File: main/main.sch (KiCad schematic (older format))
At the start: 9 parts, among them J1 DIN41524-MIDI-IN, J2 AudioJack3, J3 Conn_02x10_Odd_Even, U1 6N138, U2 EFM32GG990F1024, U3 EFM32GG990F1024

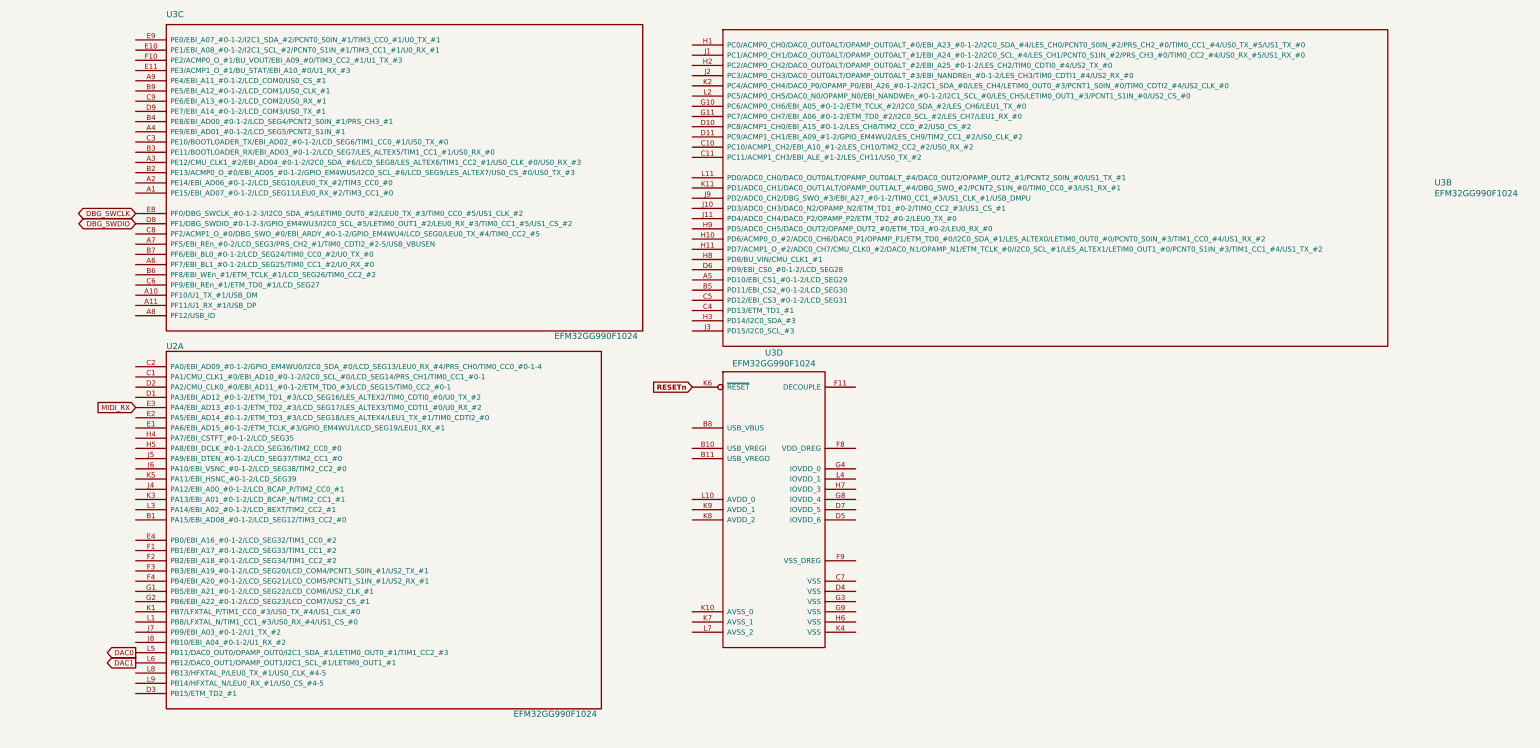
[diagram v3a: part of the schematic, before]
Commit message: Add EFM32GG component library
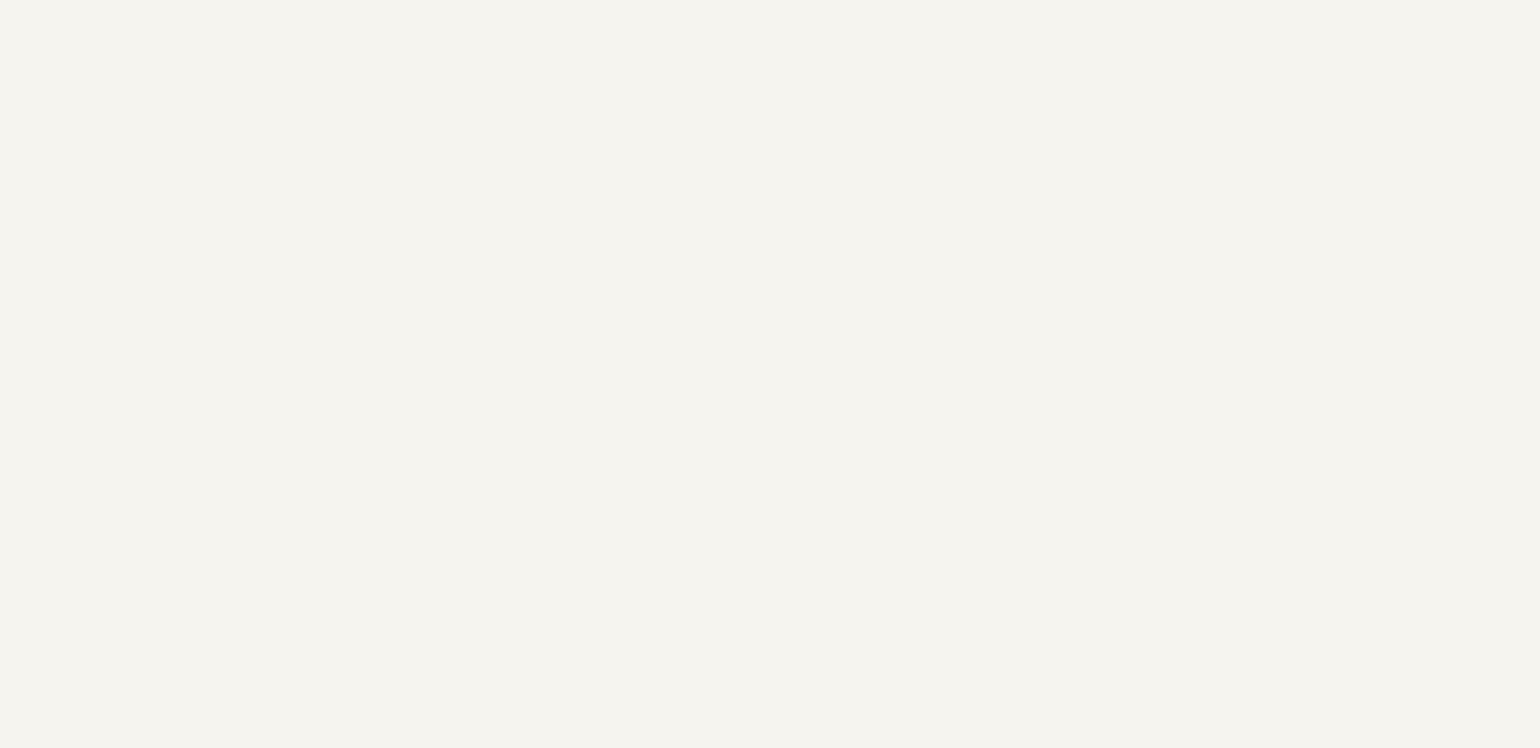
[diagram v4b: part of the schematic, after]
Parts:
- removed U2, U3: EFM32GG990F1024, symbol energymicro-efm32:EFM32GG990F1024
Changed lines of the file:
@@
 Wire Wire Line
 	2700 4800 2800 4800
-$Comp
-L energymicro-efm32:EFM32GG990F1024 U2
-U 1 1 6137537F
-P 11850 4000
-F 0 "U2" H 12150 4200 60  0000 L CNN
-F 1 "EFM32GG990F1024" H 15550 600 60  0000 L CNN
-F 2 "" H 11850 4000 50  0001 C CNN
-F 3 "http://www.energymicro.com/downloads/datasheets" H 11850 4000 50  0001 C CNN
-	1    11850 4000
-	1    0    0    -1
-$EndComp
-Text GLabel 11850 6800 0    50   Output ~ 0
-DAC0
-Text GLabel 11850 6900 0    50   Output ~ 0
-DAC1
 Text GLabel 2800 4600 0    50   Input ~ 0
 DAC0
@@
 Wire Notes Line
 	4250 3400 4250 550
-Text GLabel 11850 4400 0    50   Input ~ 0
-MIDI_RX
-$Comp
-L energymicro-efm32:EFM32GG990F1024 U3
-U 3 1 61390272
-P 11850 800
-F 0 "U3" H 12150 1050 60  0000 L CNN
-F 1 "EFM32GG990F1024" H 15950 -2100 60  0000 L CNN
-F 2 "" H 11850 800 50  0001 C CNN
-F 3 "http://www.energymicro.com/downloads/datasheets" H 11850 800 50  0001 C CNN
-	3    11850 800
-	1    0    0    -1
-$EndComp
-Text GLabel 11850 2500 0    50   BiDi ~ 0
-DBG_SWCLK
-Text GLabel 11850 2600 0    50   BiDi ~ 0
-DBG_SWDIO
 Wire Notes Line
 	550  7650 4250 7650
@@
 NoConn ~ 2750 6600
 NoConn ~ 2750 6900
-$Comp
-L energymicro-efm32:EFM32GG990F1024 U3
-U 2 1 613B0438
-P 17300 850
-F 0 "U3" H 24568 -497 60  0000 L CNN
-F 1 "EFM32GG990F1024" H 24568 -603 60  0000 L CNN
-F 2 "" H 17300 850 50  0001 C CNN
-F 3 "http://www.energymicro.com/downloads/datasheets" H 17300 850 50  0001 C CNN
-	2    17300 850
-	1    0    0    -1
-$EndComp
-$Comp
-L energymicro-efm32:EFM32GG990F1024 U3
-U 4 1 613B35C7
-P 17300 4200
-F 0 "U3" H 18100 4537 60  0000 C CNN
-F 1 "EFM32GG990F1024" H 18100 4431 60  0000 C CNN
-F 2 "" H 17300 4200 50  0001 C CNN
-F 3 "http://www.energymicro.com/downloads/datasheets" H 17300 4200 50  0001 C CNN
-	4    17300 4200
-	1    0    0    -1
-$EndComp
-Text GLabel 17300 4200 0    50   Input ~ 10
-RESETn
 Text GLabel 2750 7100 0    50   Output ~ 10
 RESETn

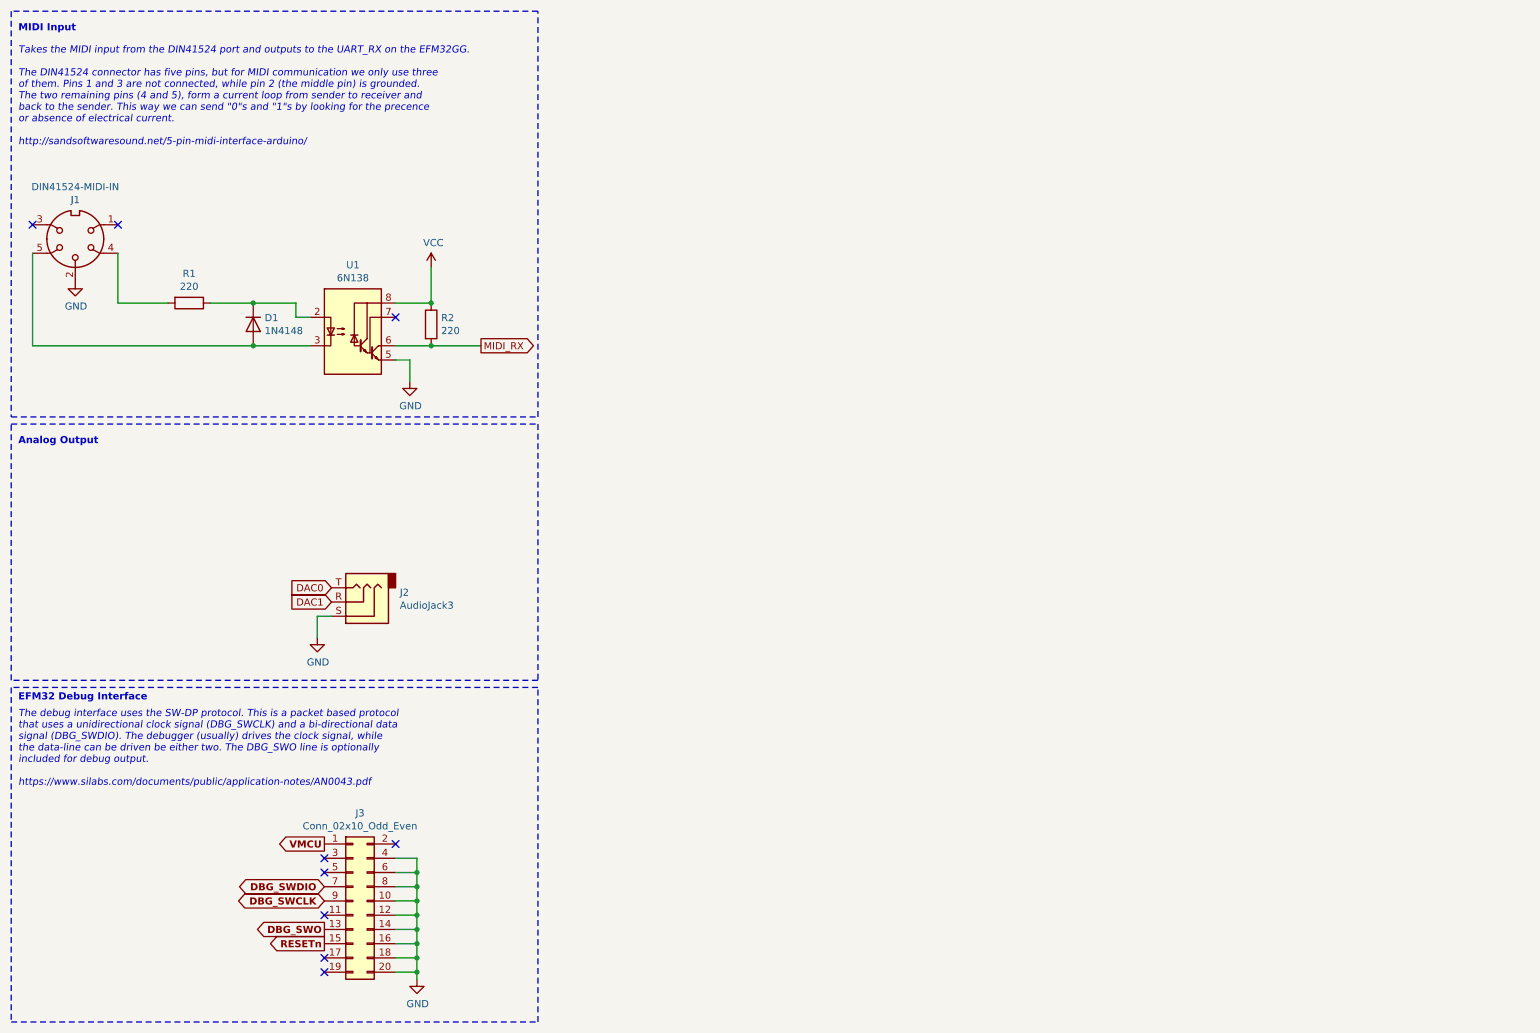
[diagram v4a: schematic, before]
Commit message: Place separate parts in hierarchical sheets, connect in main schematic
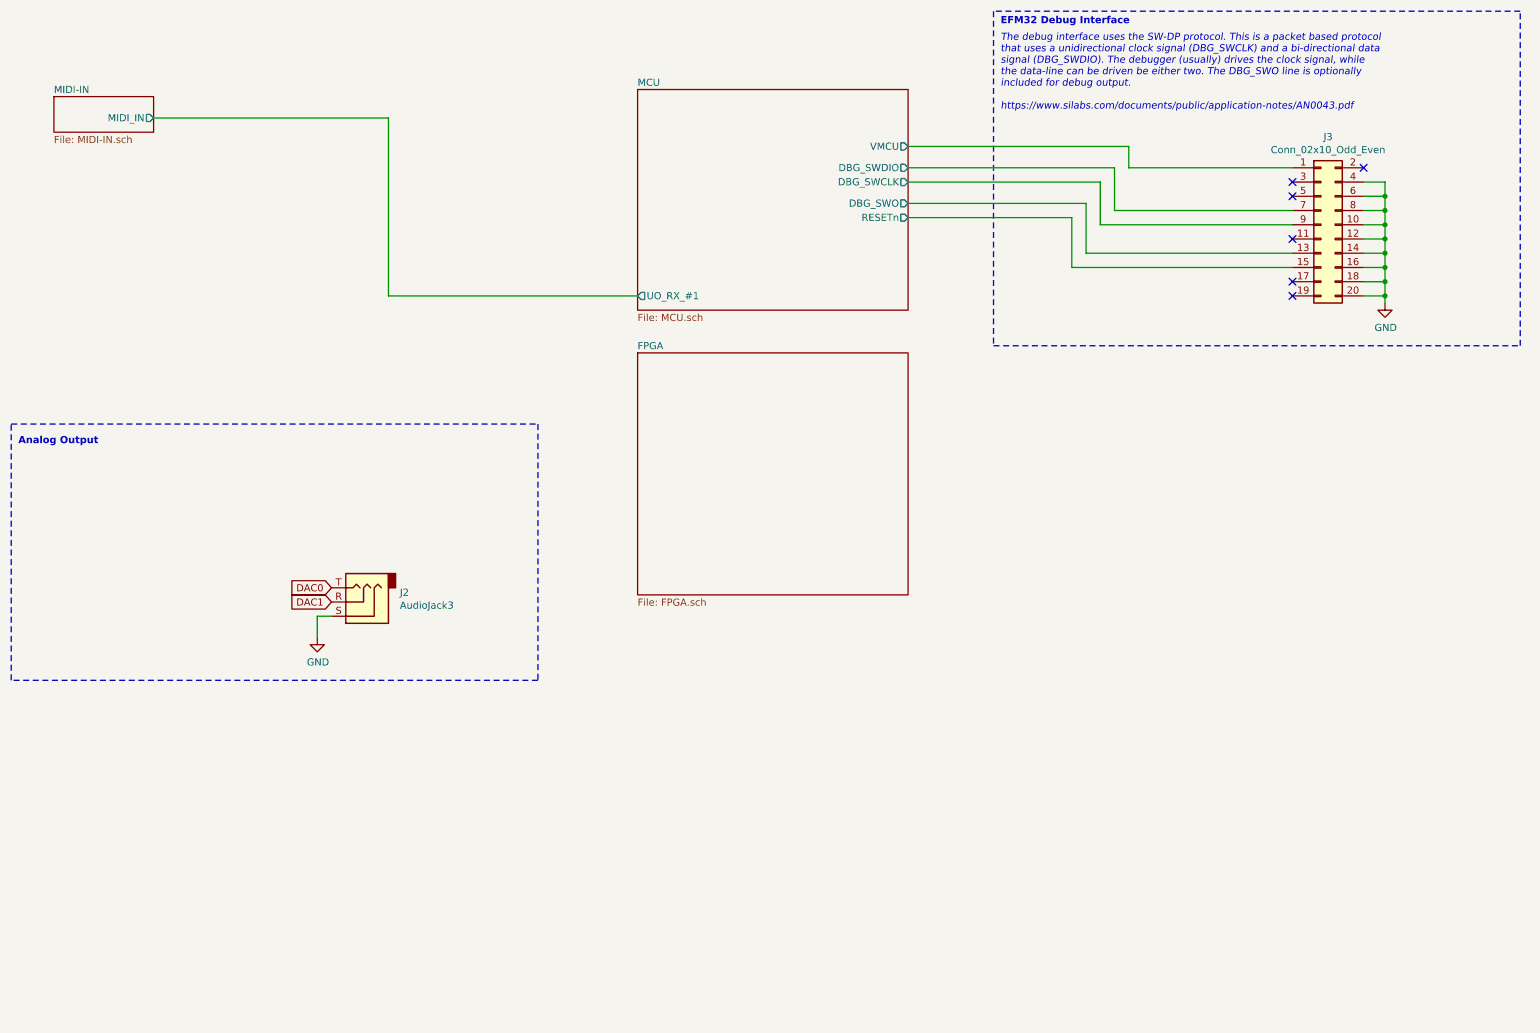
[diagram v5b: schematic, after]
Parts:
- removed D1: 1N4148, Diode_THT:D_DO-35_SOD27_P7.62mm_Horizontal, symbol Diode:1N4148
- removed J1: DIN41524-MIDI-IN, symbol MIDI:DIN41524-MIDI-IN
- removed R1, R2: 220, symbol Device:R
- removed U1: 6N138, symbol Isolator:6N138
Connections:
- net DBG_SWCLK renamed MCU/DBG_SWCLK
- net DBG_SWDIO renamed MCU/DBG_SWDIO
- net DBG_SWO renamed MCU/DBG_SWO
- net RESETn renamed MCU/RESETn
- net VMCU renamed MCU/VMCU
- no-connect marks 9 -> 6
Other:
- note removed: "MIDI Input"
- note removed: "Takes the MIDI input from the DIN41524 port and outputs to the UART_RX on the EFM32GG.\n\nThe DIN41524 connector has five pins, but for MIDI communication we only use three\nof them. Pins 1 and 3 are not connected, while pin 2 (the middle pin) is grounded.\nThe two remaining pins (4 and 5), form a current loop from sender to receiver and\nback to the sender. This way we can send "0"s and "1"s by 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"
- moved on the sheet: J3
